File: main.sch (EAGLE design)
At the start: 49 parts, among them U2 SN65HVD32_D_8

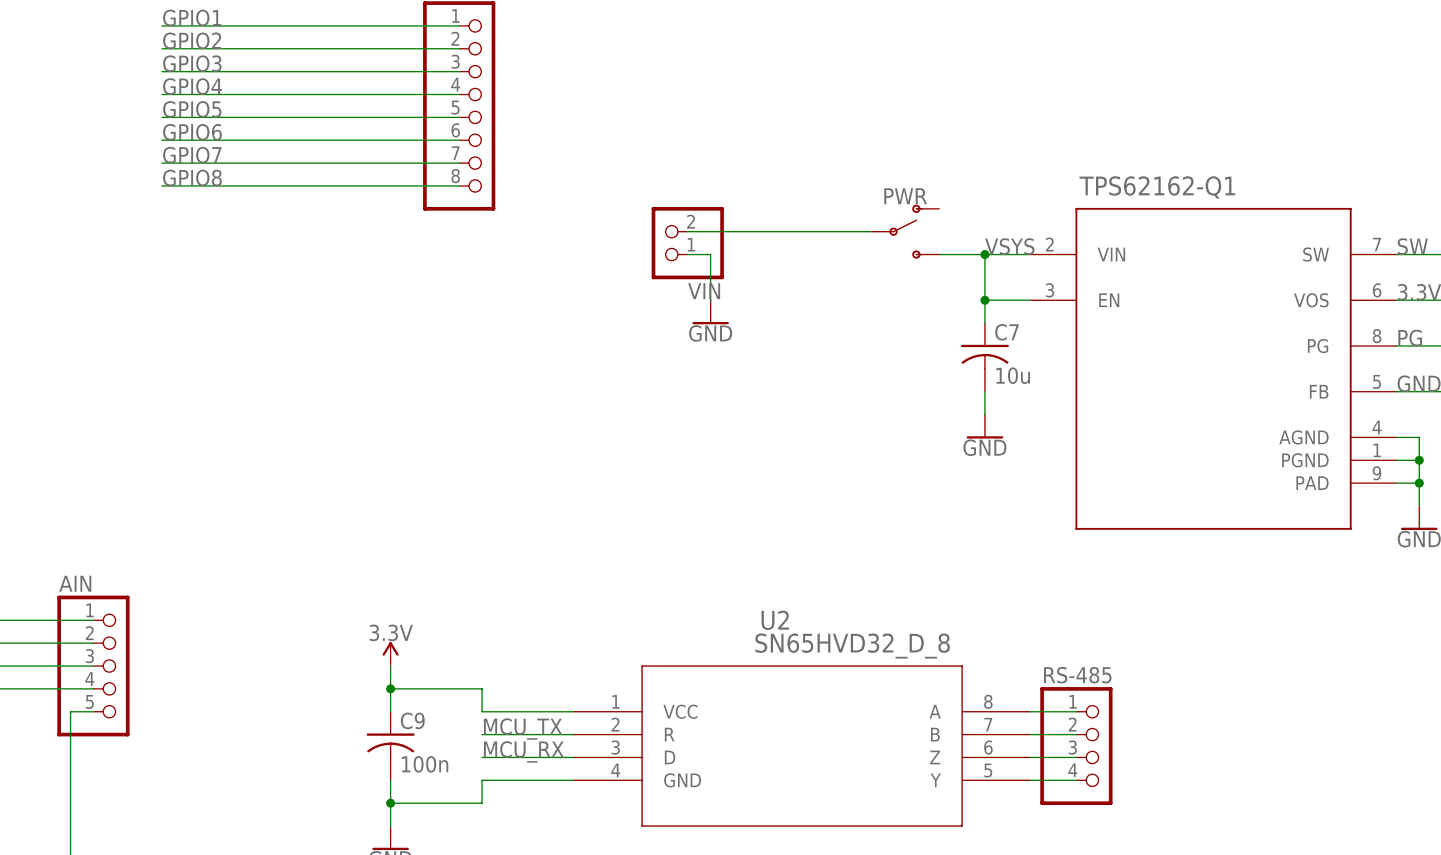
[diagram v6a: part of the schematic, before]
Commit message: Labeled compenents added logos
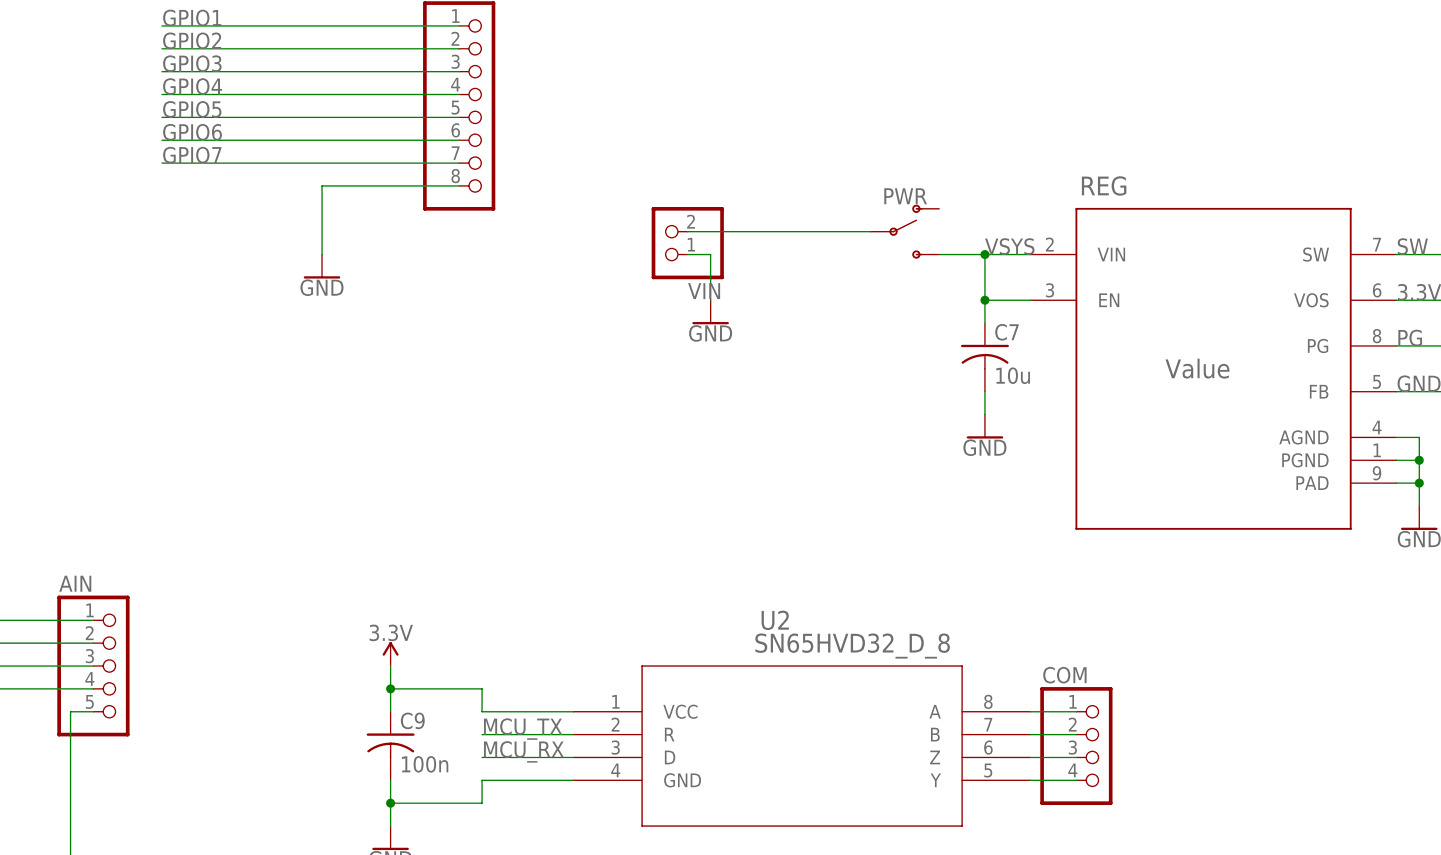
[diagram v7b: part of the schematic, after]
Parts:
- REG: value TPS62162QDSGRQ1 -> Value
- renumbered RS-485 to COM, TPS62162-Q1 to REG
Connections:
- net N$11 renamed B
- net N$12 renamed Z
- net N$13 renamed Y
- net N$6 renamed A
- net GND: now also GPIO.8
- net GPIO8: no longer GPIO.8
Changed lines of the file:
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@@
 <part name="GND24" library="SparkFun-PowerSymbols" deviceset="GND" device=""/>
 <part name="U2" library="SN65HVD32" deviceset="SN65HVD32_D_8" device=""/>
-<part name="RS-485" library="pinhead" deviceset="PINHD-1X4" device=""/>
+<part name="COM" library="pinhead" deviceset="PINHD-1X4" device=""/>
 <part name="AIN" library="pinhead" deviceset="PINHD-1X5" device=""/>
 <part name="VDUC" library="pinhead" deviceset="PINHD-1X2" device=""/>
@@
 <part name="R28" library="resistor" deviceset="R-US_" device="R0603" value="64.9"/>
 <part name="LED1" library="adafruit" deviceset="LED" device="CHIPLED_0603" value="2V @ 20mA"/>
-<part name="TPS62162-Q1" library="TPS62162-Q1" deviceset="TPS62162QDSGRQ1" device="" value=""/>
+<part name="REG" library="TPS62162-Q1" deviceset="TPS62162QDSGRQ1" device="" value="Value"/>
 <part name="GND6" library="SparkFun-PowerSymbols" deviceset="GND" device=""/>
 <part name="GND7" library="SparkFun-PowerSymbols" deviceset="GND" device=""/>
@@
 <part name="SUPPLY12" library="SparkFun-PowerSymbols" deviceset="3.3V" device=""/>
 <part name="R2" library="resistor" deviceset="R-US_" device="R0603" value="10k"/>
+<part name="GND20" library="SparkFun-PowerSymbols" deviceset="GND" device=""/>
 </parts>
 <sheets>
@@
 <instance part="GND24" gate="1" x="447.04" y="73.66"/>
 <instance part="U2" gate="A" x="467.36" y="88.9"/>
-<instance part="RS-485" gate="A" x="525.78" y="83.82"/>
+<instance part="COM" gate="A" x="525.78" y="83.82"/>
 <instance part="AIN" gate="A" x="416.56" y="93.98"/>
 <instance part="VDUC" gate="G$1" x="393.7" y="165.1"/>
@@
 <instance part="R28" gate="G$1" x="106.68" y="91.44" rot="R180"/>
 <instance part="LED1" gate="G$1" x="93.98" y="91.44" rot="R90"/>
-<instance part="TPS62162-Q1" gate="A" x="538.48" y="127" smashed="yes">
+<instance part="REG" gate="A" x="538.48" y="127" smashed="yes">
 <attribute name="NAME" x="523.5956" y="146.2786" size="2.0828" layer="95" ratio="6" rot="SR0"/>
 <attribute name="VALUE" x="533.1206" y="125.9586" size="2.0828" layer="96" ratio="6" rot="SR0"/>
@@
 <instance part="SUPPLY12" gate="G$1" x="243.84" y="114.3"/>
 <instance part="R2" gate="G$1" x="243.84" y="106.68" rot="R270"/>
+<instance part="GND20" gate="1" x="439.42" y="137.16"/>
 </instances>
 <busses>
@@
 <wire x1="601.98" y1="139.7" x2="601.98" y2="142.24" width="0.1524" layer="91"/>
 <junction x="601.98" y="139.7"/>
-<pinref part="TPS62162-Q1" gate="A" pin="VOS"/>
+<pinref part="REG" gate="A" pin="VOS"/>
 <wire x1="558.8" y1="134.62" x2="584.2" y2="134.62" width="0.1524" layer="91"/>
 <wire x1="584.2" y1="139.7" x2="584.2" y2="134.62" width="0.1524" layer="91"/>
@@
 </segment>
 <segment>
-<pinref part="TPS62162-Q1" gate="A" pin="PGND"/>
+<pinref part="REG" gate="A" pin="PGND"/>
 <wire x1="558.8" y1="116.84" x2="561.34" y2="116.84" width="0.1524" layer="91"/>
 <wire x1="561.34" y1="116.84" x2="561.34" y2="114.3" width="0.1524" layer="91"/>
@@
 <wire x1="561.34" y1="116.84" x2="561.34" y2="119.38" width="0.1524" layer="91"/>
 <junction x="561.34" y="116.84"/>
-<pinref part="TPS62162-Q1" gate="A" pin="AGND"/>
+<pinref part="REG" gate="A" pin="AGND"/>
 <wire x1="561.34" y1="119.38" x2="558.8" y2="119.38" width="0.1524" layer="91"/>
 <pinref part="GND6" gate="1" pin="GND"/>
-<pinref part="TPS62162-Q1" gate="A" pin="PAD"/>
+<pinref part="REG" gate="A" pin="PAD"/>
 <wire x1="558.8" y1="114.3" x2="561.34" y2="114.3" width="0.1524" layer="91"/>
 <junction x="561.34" y="114.3"/>
@@
 <pinref part="GND8" gate="1" pin="GND"/>
 <wire x1="601.98" y1="121.92" x2="568.96" y2="121.92" width="0.1524" layer="91"/>
-<pinref part="TPS62162-Q1" gate="A" pin="FB"/>
+<pinref part="REG" gate="A" pin="FB"/>
 <wire x1="558.8" y1="124.46" x2="568.96" y2="124.46" width="0.1524" layer="91"/>
 <wire x1="568.96" y1="121.92" x2="568.96" y2="124.46" width="0.1524" layer="91"/>
@@
 <wire x1="256.54" y1="96.52" x2="254" y2="96.52" width="0.1524" layer="91"/>
 </segment>
+<segment>
+<pinref part="GPIO" gate="A" pin="8"/>
+<wire x1="454.66" y1="147.32" x2="439.42" y2="147.32" width="0.1524" layer="91"/>
+<wire x1="439.42" y1="147.32" x2="439.42" y2="139.7" width="0.1524" layer="91"/>
+<pinref part="GND20" gate="1" pin="GND"/>
+</segment>
 </net>
 <net name="VDDCORE" class="0">
@@
 </segment>
 </net>
-<net name="N$6" class="0">
+<net name="A" class="0">
 <segment>
 <pinref part="U2" gate="A" pin="A"/>
-<pinref part="RS-485" gate="A" pin="1"/>
+<pinref part="COM" gate="A" pin="1"/>
 <wire x1="518.16" y1="88.9" x2="523.24" y2="88.9" width="0.1524" layer="91"/>
 </segment>
 </net>
-<net name="N$11" class="0">
+<net name="B" class="0">
 <segment>
 <pinref part="U2" gate="A" pin="B"/>
-<pinref part="RS-485" gate="A" pin="2"/>
+<pinref part="COM" gate="A" pin="2"/>
 <wire x1="518.16" y1="86.36" x2="523.24" y2="86.36" width="0.1524" layer="91"/>
 </segment>
 </net>
-<net name="N$12" class="0">
+<net name="Z" class="0">
 <segment>
 <pinref part="U2" gate="A" pin="Z"/>
-<pinref part="RS-485" gate="A" pin="3"/>
+<pinref part="COM" gate="A" pin="3"/>
 <wire x1="518.16" y1="83.82" x2="523.24" y2="83.82" width="0.1524" layer="91"/>
 </segment>
 </net>
-<net name="N$13" class="0">
+<net name="Y" class="0">
 <segment>
 <pinref part="U2" gate="A" pin="Y"/>
-<pinref part="RS-485" gate="A" pin="4"/>
+<pinref part="COM" gate="A" pin="4"/>
 <wire x1="518.16" y1="81.28" x2="523.24" y2="81.28" width="0.1524" layer="91"/>
 </segment>
@@
 </segment>
 <segment>
-<pinref part="TPS62162-Q1" gate="A" pin="VIN"/>
+<pinref part="REG" gate="A" pin="VIN"/>
 <wire x1="518.16" y1="139.7" x2="513.08" y2="139.7" width="0.1524" layer="91"/>
-<pinref part="TPS62162-Q1" gate="A" pin="EN"/>
+<pinref part="REG" gate="A" pin="EN"/>
 <wire x1="518.16" y1="134.62" x2="513.08" y2="134.62" width="0.1524" layer="91"/>
 <wire x1="513.08" y1="134.62" x2="513.08" y2="139.7" width="0.1524" layer="91"/>
@@
 <net name="GPIO8" class="0">
 <segment>
-<wire x1="454.66" y1="147.32" x2="421.64" y2="147.32" width="0.1524" layer="91"/>
-<label x="421.64" y="147.32" size="1.778" layer="95"/>
-<pinref part="GPIO" gate="A" pin="8"/>
-</segment>
-<segment>
 <pinref part="MCU" gate="G$1" pin="PA18(SER1:2+)"/>
 <label x="205.74" y="99.06" size="1.778" layer="95"/>
@@
 <net name="PG" class="0">
 <segment>
-<pinref part="TPS62162-Q1" gate="A" pin="PG"/>
+<pinref part="REG" gate="A" pin="PG"/>
 <wire x1="558.8" y1="129.54" x2="571.5" y2="129.54" width="0.1524" layer="91"/>
 <wire x1="571.5" y1="129.54" x2="571.5" y2="127" width="0.1524" layer="91"/>
@@
 <net name="SW" class="0">
 <segment>
-<pinref part="TPS62162-Q1" gate="A" pin="SW"/>
+<pinref part="REG" gate="A" pin="SW"/>
 <pinref part="L1" gate="G$1" pin="1"/>
 <wire x1="558.8" y1="139.7" x2="563.88" y2="139.7" width="0.1524" layer="91"/>

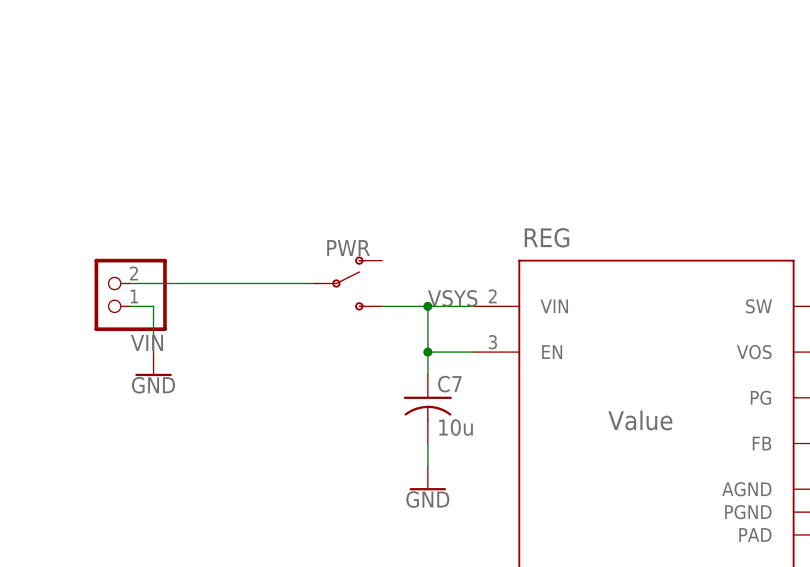
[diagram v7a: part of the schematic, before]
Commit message: Small switch adjustment, and render update for this change
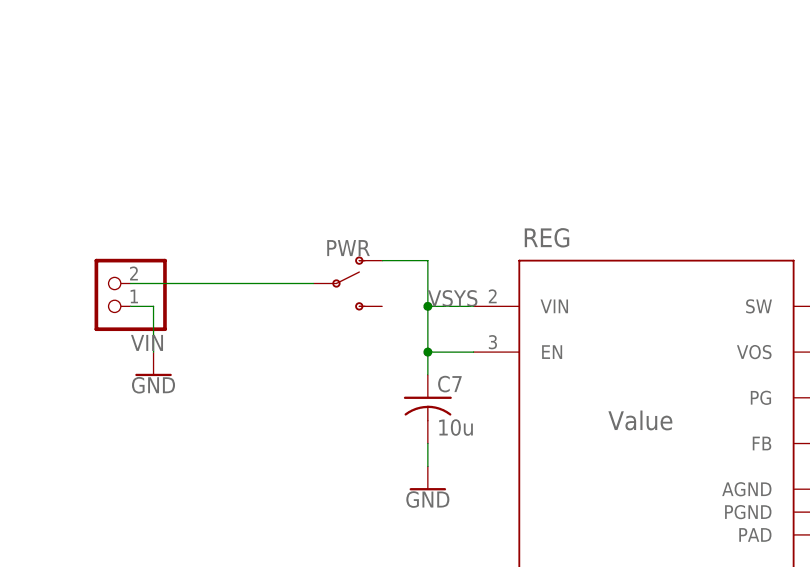
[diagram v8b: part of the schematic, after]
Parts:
- PWR: device SparkFun-Switches:SWITCH-SPDT-SMD-AYZ0202 -> SparkFun-Switches:SWITCH-SPDT-PTH-11.6X4.0MM
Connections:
- net VSYS: now also PWR.O; no longer PWR.S
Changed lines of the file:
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@@
 <part name="GND8" library="SparkFun-PowerSymbols" deviceset="GND" device=""/>
 <part name="SUPPLY14" library="SparkFun-PowerSymbols" deviceset="3.3V" device=""/>
-<part name="PWR" library="SparkFun-Switches" deviceset="SWITCH-SPDT" device="-SMD-AYZ0202"/>
 <part name="C7" library="resistor" deviceset="C-US" device="C0603" value="10u"/>
 <part name="VIN" library="pinhead" deviceset="PINHD-1X2" device=""/>
@@
 <part name="R2" library="resistor" deviceset="R-US_" device="R0603" value="10k"/>
 <part name="GND20" library="SparkFun-PowerSymbols" deviceset="GND" device=""/>
+<part name="PWR" library="SparkFun-Switches" deviceset="SWITCH-SPDT" device="-PTH-11.6X4.0MM"/>
 </parts>
 <sheets>
@@
 <instance part="GND8" gate="1" x="601.98" y="116.84"/>
 <instance part="SUPPLY14" gate="G$1" x="601.98" y="142.24"/>
-<instance part="PWR" gate="1" x="502.92" y="142.24"/>
 <instance part="C7" gate="G$1" x="513.08" y="129.54"/>
 <instance part="VIN" gate="G$1" x="477.52" y="142.24" rot="R180"/>
@@
 <instance part="R2" gate="G$1" x="243.84" y="106.68" rot="R270"/>
 <instance part="GND20" gate="1" x="439.42" y="137.16"/>
+<instance part="PWR" gate="1" x="502.92" y="142.24"/>
 </instances>
 <busses>
@@
 <label x="513.08" y="139.7" size="1.778" layer="95"/>
 <pinref part="C7" gate="G$1" pin="1"/>
-<pinref part="PWR" gate="1" pin="S"/>
-<wire x1="513.08" y1="139.7" x2="508" y2="139.7" width="0.1524" layer="91"/>
+<pinref part="PWR" gate="1" pin="O"/>
+<wire x1="513.08" y1="139.7" x2="513.08" y2="144.78" width="0.1524" layer="91"/>
+<wire x1="513.08" y1="144.78" x2="508" y2="144.78" width="0.1524" layer="91"/>
 <junction x="513.08" y="139.7"/>
 </segment>
@@
 <net name="N$9" class="0">
 <segment>
-<pinref part="PWR" gate="1" pin="P"/>
 <wire x1="500.38" y1="142.24" x2="480.06" y2="142.24" width="0.1524" layer="91"/>
 <pinref part="VIN" gate="G$1" pin="2"/>
-</segment>
-</net>
+<pinref part="PWR" gate="1" pin="P"/>
+</segment>
+</net>
